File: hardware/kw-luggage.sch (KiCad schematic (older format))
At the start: 22 parts

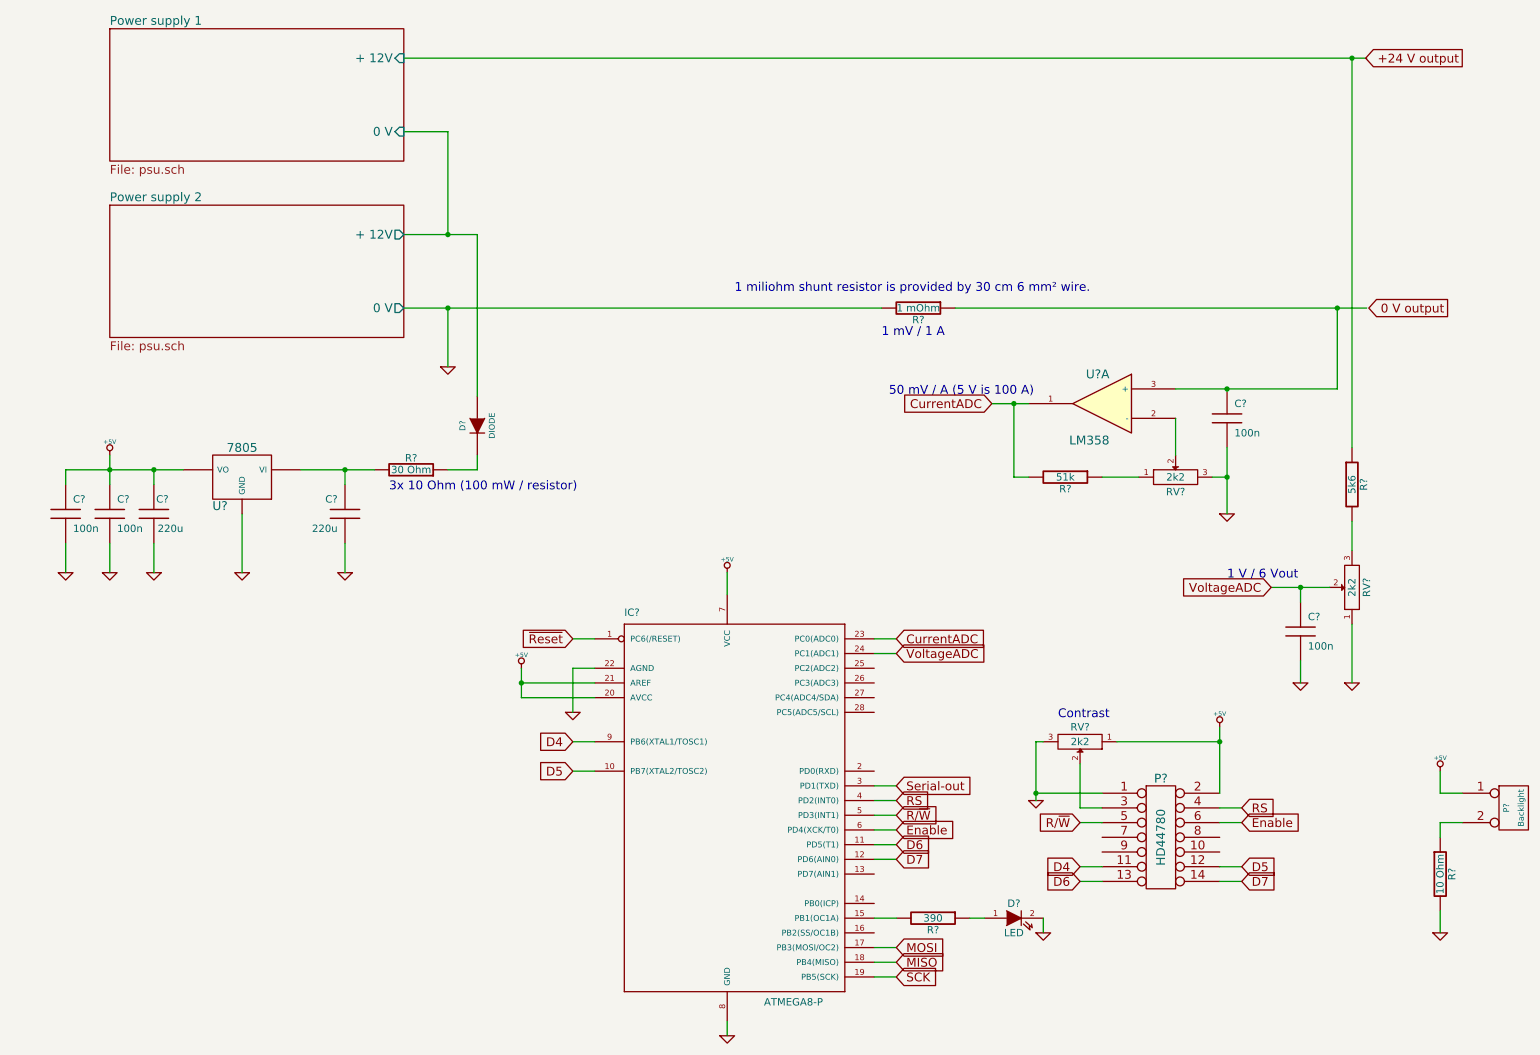
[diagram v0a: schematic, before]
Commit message: Added ISP header to schematic
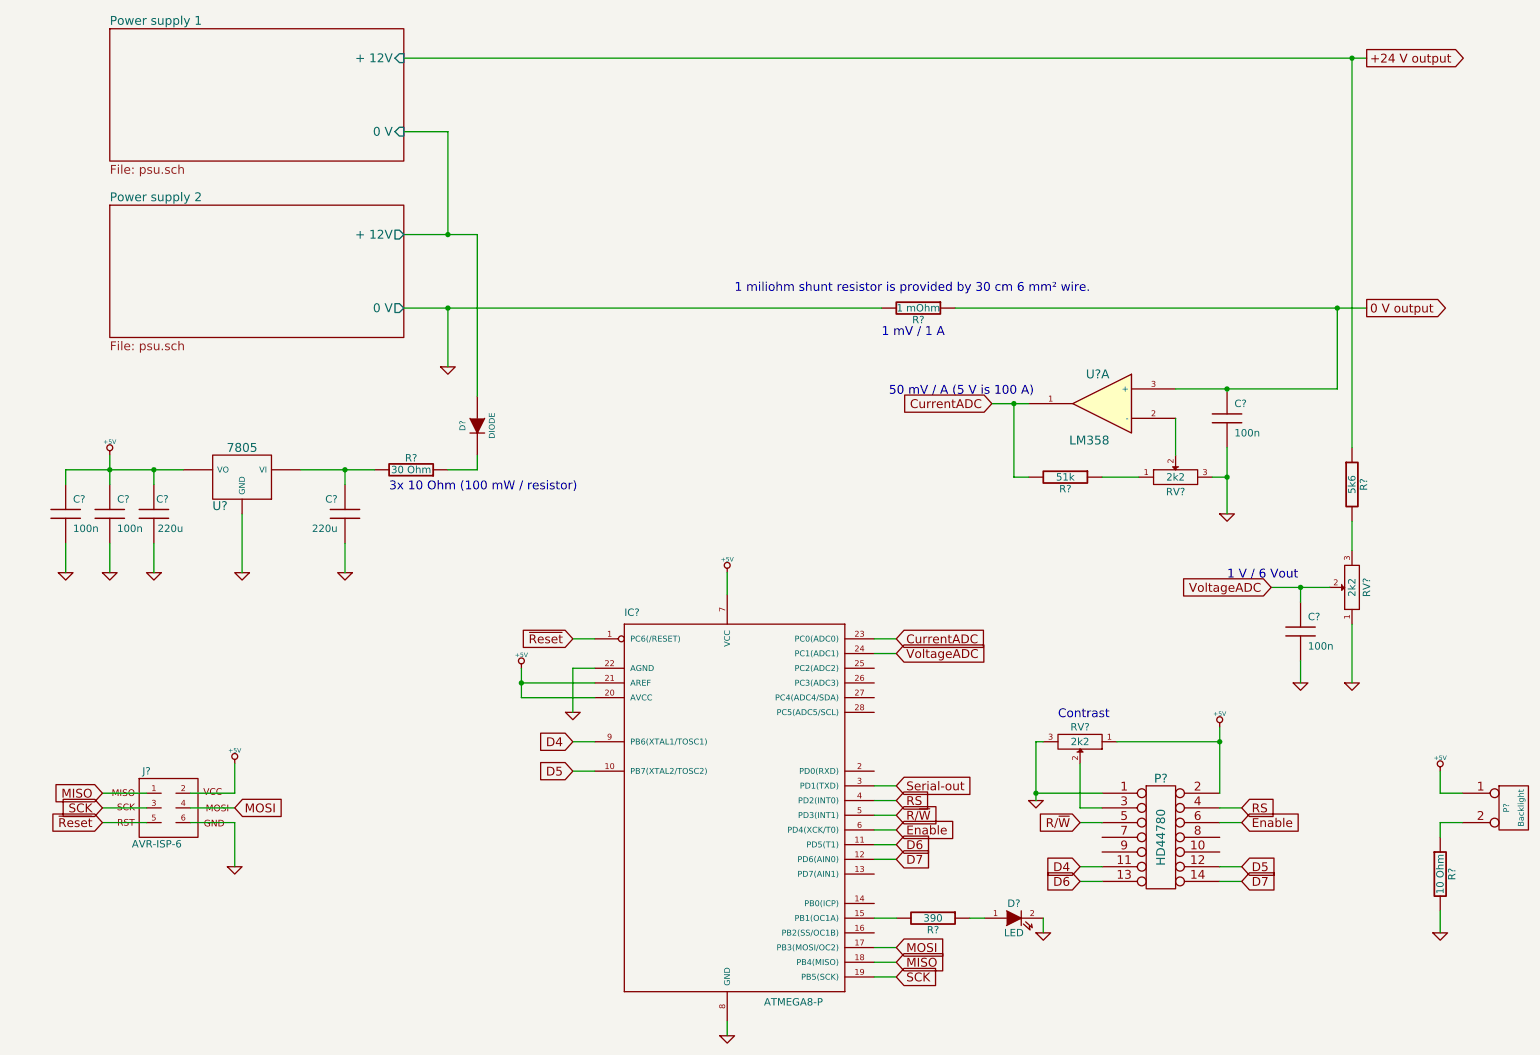
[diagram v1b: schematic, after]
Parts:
- added J?: AVR-ISP-6, AVR-ISP-6, symbol AVR-ISP-6
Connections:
- net Power supply 1/+ 12V is gone; now on net +24 V output: R?.1
- net +5V: now also J?.2
- net 0 V output: now also C?.1, R?.1, U?.3 (+)
- net GND: now also J?.6
- net MISO: now also J?.1
- net MOSI: now also J?.4
- net SCK: now also J?.3
- net ~Reset: now also J?.5
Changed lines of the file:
@@
-EESchema Schematic File Version 2  date 2012-05-20T22:26:10 CEST
+EESchema Schematic File Version 2  date 2012-05-21T21:48:12 CEST
 LIBS:power
 LIBS:device
@@
 LIBS:contrib
 LIBS:valves
-EELAYER 43  0
+LIBS:kw-luggage-cache
+EELAYER 25  0
 EELAYER END
 $Descr A4 11700 8267
@@
 Sheet 1 3
 Title ""
-Date "20 may 2012"
+Date "21 may 2012"
 Rev ""
 Comp ""
@@
 $EndDescr
 Wire Wire Line
+	1250 6000 950  6000
+Wire Wire Line
+	1250 6200 950  6200
+Wire Wire Line
+	1850 5800 1850 6000
+Wire Wire Line
+	1850 6000 1550 6000
+Wire Wire Line
 	6350 6850 6200 6850
 Wire Wire Line
@@
 Wire Wire Line
 	6950 6850 6850 6850
+Wire Wire Line
+	1850 6100 1550 6100
+Wire Wire Line
+	1850 6500 1850 6200
+Wire Wire Line
+	1850 6200 1550 6200
+Wire Wire Line
+	950  6100 1250 6100
+Text GLabel 1850 6100 2    60   Input ~ 0
+MOSI
+$Comp
+L GND #PWR?
+U 1 1 4FBA9B69
+P 1850 6500
+F 0 "#PWR?" H 1850 6500 30  0001 C CNN
+F 1 "GND" H 1850 6430 30  0001 C CNN
+	1    1850 6500
+	1    0    0    -1
+$EndComp
+$Comp
+L +5V #PWR?
+U 1 1 4FBA9B65
+P 1850 5800
+F 0 "#PWR?" H 1850 5890 20  0001 C CNN
+F 1 "+5V" H 1850 5890 30  0000 C CNN
+	1    1850 5800
+	1    0    0    -1
+$EndComp
+Text GLabel 950  6200 0    60   Input ~ 0
+~Reset
+Text GLabel 950  6100 0    60   Input ~ 0
+SCK
+Text GLabel 950  6000 0    60   Input ~ 0
+MISO
+$Comp
+L AVR-ISP-6 J?
+U 1 1 4FBA9B2E
+P 1400 6100
+F 0 "J?" H 1250 6350 50  0000 C CNN
+F 1 "AVR-ISP-6" H 1150 5825 50  0000 L BNN
+F 2 "AVR-ISP-6" V 900 6100 50  0001 C CNN
+	1    1400 6100
+	1    0    0    -1
+$EndComp
 $Comp
 L GND #PWR?
@@
 	0    1    1    0
 $EndComp
-Text GLabel 10200 1000 0    60   Output ~ 0
+Text GLabel 9550 1000 2    60   Output ~ 0
 +24 V output
-Text GLabel 10100 2700 0    60   Output ~ 0
+Text GLabel 9550 2700 2    60   Output ~ 0
 0 V output
 $Sheet

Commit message: Switched to an lcd library that actually works
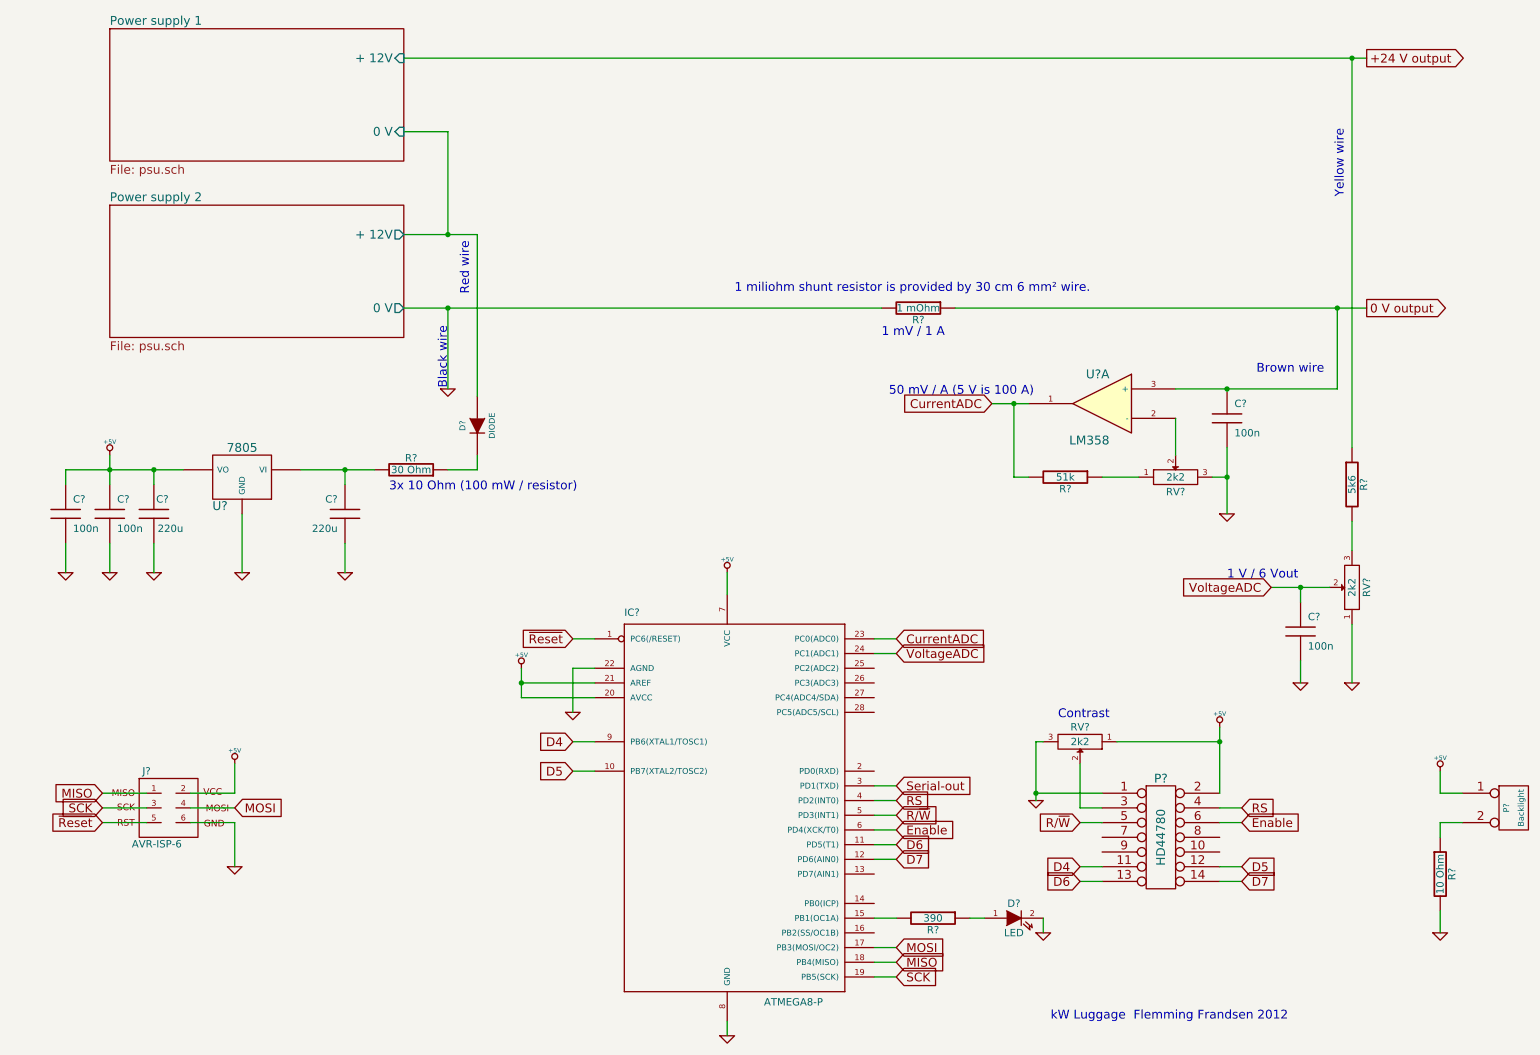
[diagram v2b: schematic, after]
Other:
- note added: "Black wire"
- note added: "Brown wire"
- note added: "Red wire"
- note added: "Yellow wire"
- note added: "kW Luggage Flemming Frandsen 2012"
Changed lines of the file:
@@
-EESchema Schematic File Version 2  date 2012-05-21T21:48:12 CEST
+EESchema Schematic File Version 2  date 2012-05-24T16:14:34 CEST
 LIBS:power
 LIBS:device
@@
 Sheet 1 3
 Title ""
-Date "21 may 2012"
+Date "24 may 2012"
 Rev ""
 Comp ""
@@
 Comment4 ""
 $EndDescr
+Text Notes 7400 7550 0    60   ~ 0
+kW Luggage  Flemming Frandsen 2012
+Text Notes 3300 3250 1    60   ~ 0
+Black wire
+Wire Wire Line
+	3300 3250 3300 2700
+Wire Wire Line
+	950  6100 1250 6100
+Wire Wire Line
+	1550 6200 1850 6200
+Wire Wire Line
+	1850 6200 1850 6500
+Wire Wire Line
+	1850 6100 1550 6100
+Wire Wire Line
+	6950 6850 6850 6850
+Wire Wire Line
+	6350 5950 6200 5950
+Wire Wire Line
+	8900 4600 9300 4600
+Wire Wire Line
+	6350 4950 6200 4950
+Wire Wire Line
+	7000 3350 7250 3350
+Wire Wire Line
+	4300 5650 4150 5650
+Wire Wire Line
+	6350 6450 6200 6450
+Wire Wire Line
+	6350 6050 6200 6050
+Wire Wire Line
+	6350 6250 6200 6250
+Wire Wire Line
+	1500 3800 700  3800
+Wire Wire Line
+	700  3800 700  3900
+Wire Wire Line
+	1000 4300 1000 4500
+Wire Wire Line
+	5200 7650 5200 7550
+Wire Wire Line
+	6350 7150 6200 7150
+Wire Wire Line
+	4150 4950 4300 4950
+Connection ~ 3800 5250
+Wire Wire Line
+	4300 5250 3800 5250
+Wire Wire Line
+	5200 4500 5200 4650
+Wire Wire Line
+	7750 6500 7600 6500
+Wire Wire Line
+	8700 6600 8550 6600
+Wire Wire Line
+	8700 6100 8550 6100
+Connection ~ 7300 6000
+Wire Wire Line
+	7350 5650 7300 5650
+Wire Wire Line
+	7300 5650 7300 6050
+Wire Wire Line
+	7850 5650 8550 5650
+Wire Wire Line
+	10050 6300 10050 6200
+Wire Wire Line
+	10050 6200 10200 6200
+Wire Wire Line
+	10200 6000 10050 6000
+Wire Wire Line
+	10050 6000 10050 5850
+Wire Wire Line
+	1300 4500 1300 4300
+Wire Wire Line
+	2600 4500 2600 4300
+Wire Wire Line
+	2800 3800 2300 3800
+Wire Wire Line
+	3500 3700 3500 3800
+Connection ~ 3300 2700
+Wire Wire Line
+	9100 4600 9100 4700
+Wire Wire Line
+	9100 5100 9100 5250
+Wire Wire Line
+	9450 3650 9450 1000
+Connection ~ 8600 3250
+Wire Wire Line
+	9350 2700 9350 3250
+Connection ~ 8600 3850
+Wire Wire Line
+	8500 3850 8600 3850
+Wire Wire Line
+	8250 3450 8250 3700
+Wire Wire Line
+	6750 2700 9550 2700
+Wire Wire Line
+	3000 2700 6250 2700
+Wire Wire Line
+	9550 1000 3000 1000
+Wire Wire Line
+	3000 1500 3300 1500
+Wire Wire Line
+	3300 1500 3300 2200
+Connection ~ 9350 2700
+Wire Wire Line
+	8600 3650 8600 4100
+Wire Wire Line
+	7750 3850 8000 3850
+Connection ~ 9450 1000
+Wire Wire Line
+	9450 4150 9450 4350
+Wire Wire Line
+	9450 4850 9450 5250
+Connection ~ 9100 4600
+Wire Wire Line
+	9350 3250 8250 3250
+Wire Wire Line
+	3000 2200 3500 2200
+Wire Wire Line
+	3500 2200 3500 3300
+Connection ~ 3300 2200
+Wire Wire Line
+	3500 3800 3300 3800
+Wire Wire Line
+	2600 3900 2600 3800
+Connection ~ 2600 3800
+Wire Wire Line
+	1900 4100 1900 4500
+Wire Wire Line
+	1300 3900 1300 3800
+Connection ~ 1300 3800
+Wire Wire Line
+	10050 6950 10050 6800
+Wire Wire Line
+	7750 6000 7300 6000
+Wire Wire Line
+	7600 5800 7600 6100
+Wire Wire Line
+	7600 6100 7750 6100
+Wire Wire Line
+	8550 6000 8550 5550
+Connection ~ 8550 5650
+Wire Wire Line
+	8700 6200 8550 6200
+Wire Wire Line
+	7600 6200 7750 6200
+Wire Wire Line
+	8550 6500 8700 6500
+Wire Wire Line
+	7600 6600 7750 6600
+Wire Wire Line
+	4300 5350 3800 5350
+Wire Wire Line
+	3800 5350 3800 5150
+Wire Wire Line
+	4150 5450 4150 5150
+Wire Wire Line
+	4150 5150 4300 5150
+Wire Wire Line
+	6350 7050 6200 7050
+Wire Wire Line
+	6350 7250 6200 7250
+Wire Wire Line
+	700  4300 700  4500
+Wire Wire Line
+	1000 3700 1000 3900
+Connection ~ 1000 3800
+Wire Wire Line
+	6200 6150 6350 6150
+Wire Wire Line
+	6200 6350 6350 6350
+Wire Wire Line
+	4150 5850 4300 5850
+Wire Wire Line
+	6350 5050 6200 5050
+Wire Wire Line
+	7250 3850 7150 3850
+Wire Wire Line
+	7150 3850 7150 3350
+Connection ~ 7150 3350
+Wire Wire Line
+	7350 6850 7350 6950
+Wire Wire Line
+	6350 6850 6200 6850
+Wire Wire Line
+	1550 6000 1850 6000
+Wire Wire Line
+	1850 6000 1850 5800
+Wire Wire Line
+	1250 6200 950  6200
 Wire Wire Line
 	1250 6000 950  6000
-Wire Wire Line
-	1250 6200 950  6200
-Wire Wire Line
-	1850 5800 1850 6000
-Wire Wire Line
-	1850 6000 1550 6000
-Wire Wire Line
-	6350 6850 6200 6850
-Wire Wire Line
-	7350 6850 7350 6950
-Connection ~ 7150 3350
-Wire Wire Line
-	7150 3350 7150 3850
-Wire Wire Line
-	7150 3850 7250 3850
-Wire Wire Line
-	6350 5050 6200 5050
-Wire Wire Line
-	4150 5850 4300 5850
-Wire Wire Line
-	6200 6350 6350 6350
-Wire Wire Line
-	6200 6150 6350 6150
-Connection ~ 1000 3800
-Wire Wire Line
-	1000 3700 1000 3900
-Wire Wire Line
-	700  4300 700  4500
-Wire Wire Line
-	6350 7250 6200 7250
-Wire Wire Line
-	6350 7050 6200 7050
-Wire Wire Line
-	4300 5150 4150 5150
-Wire Wire Line
-	4150 5150 4150 5450
-Wire Wire Line
-	3800 5150 3800 5350
-Wire Wire Line
-	3800 5350 4300 5350
-Wire Wire Line
-	7600 6600 7750 6600
-Wire Wire Line
-	8550 6500 8700 6500
-Wire Wire Line
-	7600 6200 7750 6200
-Wire Wire Line
-	8700 6200 8550 6200
-Connection ~ 8550 5650
-Wire Wire Line
-	8550 6000 8550 5550
-Wire Wire Line
-	7750 6100 7600 6100
-Wire Wire Line
-	7600 6100 7600 5800
-Wire Wire Line
-	7750 6000 7300 6000
-Wire Wire Line
-	10050 6950 10050 6800
-Connection ~ 1300 3800
-Wire Wire Line
-	1300 3900 1300 3800
-Wire Wire Line
-	1900 4100 1900 4500
-Connection ~ 2600 3800
-Wire Wire Line
-	2600 3900 2600 3800
-Wire Wire Line
-	3300 3800 3500 3800
-Connection ~ 3300 2200
-Wire Wire Line
-	3500 3300 3500 2200
-Wire Wire Line
-	3500 2200 3000 2200
-Wire Wire Line
-	8250 3250 9350 3250
-Connection ~ 9100 4600
-Wire Wire Line
-	9450 4850 9450 5250
-Wire Wire Line
-	9450 4150 9450 4350
-Connection ~ 9450 1000
-Wire Wire Line
-	7750 3850 8000 3850
-Wire Wire Line
-	8600 3650 8600 4100
-Connection ~ 9350 2700
-Wire Wire Line
-	3300 2200 3300 1500
-Wire Wire Line
-	3300 1500 3000 1500
-Wire Wire Line
-	9550 1000 3000 1000
-Wire Wire Line
-	3000 2700 6250 2700
-Wire Wire Line
-	6750 2700 9550 2700
-Wire Wire Line
-	8250 3450 8250 3700
-Wire Wire Line
-	8500 3850 8600 3850
-Connection ~ 8600 3850
-Wire Wire Line
-	9350 3250 9350 2700
-Connection ~ 8600 3250
-Wire Wire Line
-	9450 3650 9450 1000
-Wire Wire Line
-	9100 5100 9100 5250
-Wire Wire Line
-	9100 4600 9100 4700
-Wire Wire Line
-	3300 3100 3300 2700
-Connection ~ 3300 2700
-Wire Wire Line
-	3500 3800 3500 3700
-Wire Wire Line
-	2800 3800 2300 3800
-Wire Wire Line
-	2600 4500 2600 4300
-Wire Wire Line
-	1300 4500 1300 4300
-Wire Wire Line
-	10050 5850 10050 6000
-Wire Wire Line
-	10050 6000 10200 6000
-Wire Wire Line
-	10200 6200 10050 6200
-Wire Wire Line
-	10050 6200 10050 6300
-Wire Wire Line
-	7850 5650 8550 5650
-Wire Wire Line
-	7300 6050 7300 5650
-Wire Wire Line
-	7300 5650 7350 5650
-Connection ~ 7300 6000
-Wire Wire Line
-	8700 6100 8550 6100
-Wire Wire Line
-	8700 6600 8550 6600
-Wire Wire Line
-	7750 6500 7600 6500
-Wire Wire Line
-	5200 4500 5200 4650
-Wire Wire Line
-	4300 5250 3800 5250
-Connection ~ 3800 5250
-Wire Wire Line
-	4150 4950 4300 4950
-Wire Wire Line
-	6350 7150 6200 7150
-Wire Wire Line
-	5200 7650 5200 7550
-Wire Wire Line
-	1000 4300 1000 4500
-Wire Wire Line
-	700  3900 700  3800
-Wire Wire Line
-	700  3800 1500 3800
-Wire Wire Line
-	6350 6250 6200 6250
-Wire Wire Line
-	6350 6050 6200 6050
-Wire Wire Line
-	6350 6450 6200 6450
-Wire Wire Line
-	4300 5650 4150 5650
-Wire Wire Line
-	7000 3350 7250 3350
-Wire Wire Line
-	6350 4950 6200 4950
-Wire Wire Line
-	8900 4600 9300 4600
-Wire Wire Line
-	6350 5950 6200 5950
-Wire Wire Line
-	6950 6850 6850 6850
-Wire Wire Line
-	1850 6100 1550 6100
-Wire Wire Line
-	1850 6500 1850 6200
-Wire Wire Line
-	1850 6200 1550 6200
-Wire Wire Line
-	950  6100 1250 6100
+Text Notes 3450 2250 3    60   ~ 0
+Red wire
+Text Notes 8800 3150 0    60   ~ 0
+Brown wire
+Text Notes 9400 1950 1    60   ~ 0
+Yellow wire
 Text GLabel 1850 6100 2    60   Input ~ 0
 MOSI
@@
 L GND #PWR?
 U 1 1 4FB94111
-P 3300 3100
-F 0 "#PWR?" H 3300 3100 30  0001 C CNN
-F 1 "GND" H 3300 3030 30  0001 C CNN
-	1    3300 3100
-	1    0    0    -1
-$EndComp
+P 3300 3250
+F 0 "#PWR?" H 3300 3250 30  0001 C CNN
+F 1 "GND" H 3300 3180 30  0001 C CNN
+	1    3300 3250
+	1    0    0    -1
+$EndComp
